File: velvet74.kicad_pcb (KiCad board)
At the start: 4 copper layers, 268 x 133.2 mm, 415 parts, among them J1 Connector, USB-TYPE-C-16P, J2 Connector, USB-TYPE-C-16P, J201 Connector, USB-TYPE-C-16P, J202 Connector, USB-TYPE-C-16P, J203 OLED 128x32, J3 OLED 128x32, SW1 BOOT, SW10 F0, SW11 F1, SW12 F2, SW13 F3, SW14 F4, SW15 F5, SW16 F6 Choc/EC11, SW2 RESET, SW20 N0, SW201 BOOT, SW202 RESET, SW21 N1, SW210 F0, SW211 F1, SW212 F2, SW213 F3, SW214 F4, SW215 F5, SW216 F6 Choc/EC11, SW22 N2, SW220 N0, SW221 N1, SW222 N2, SW223 N3, SW224 N4, SW225 N5, SW23 N3, SW230 T0, SW231 T1, SW232 T2, SW233 T3, SW234 T4, SW235 T5, SW24 N4, SW240 H0, SW241 H1, SW242 H2, SW243 H3, SW244 H4, SW245 H5, SW25 N5, SW250 B0, SW251 B1, SW252 B2, SW253 B3, SW254 B4, SW255 B5, SW260 TH0, SW261 TH1, SW262 TH2, SW263 TH3, SW264 TH4, SW265 TH5 Choc/EC11, SW30 T0, SW31 T1, SW32 T2, SW33 T3, SW34 T4, SW35 T5, SW40 H0, SW41 H1, SW42 H2, SW43 H3, SW44 H4, SW45 H5, SW50 B0, SW51 B1, SW52 B2, SW53 B3, SW54 B4, SW55 B5, SW60 TH0, SW61 TH1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

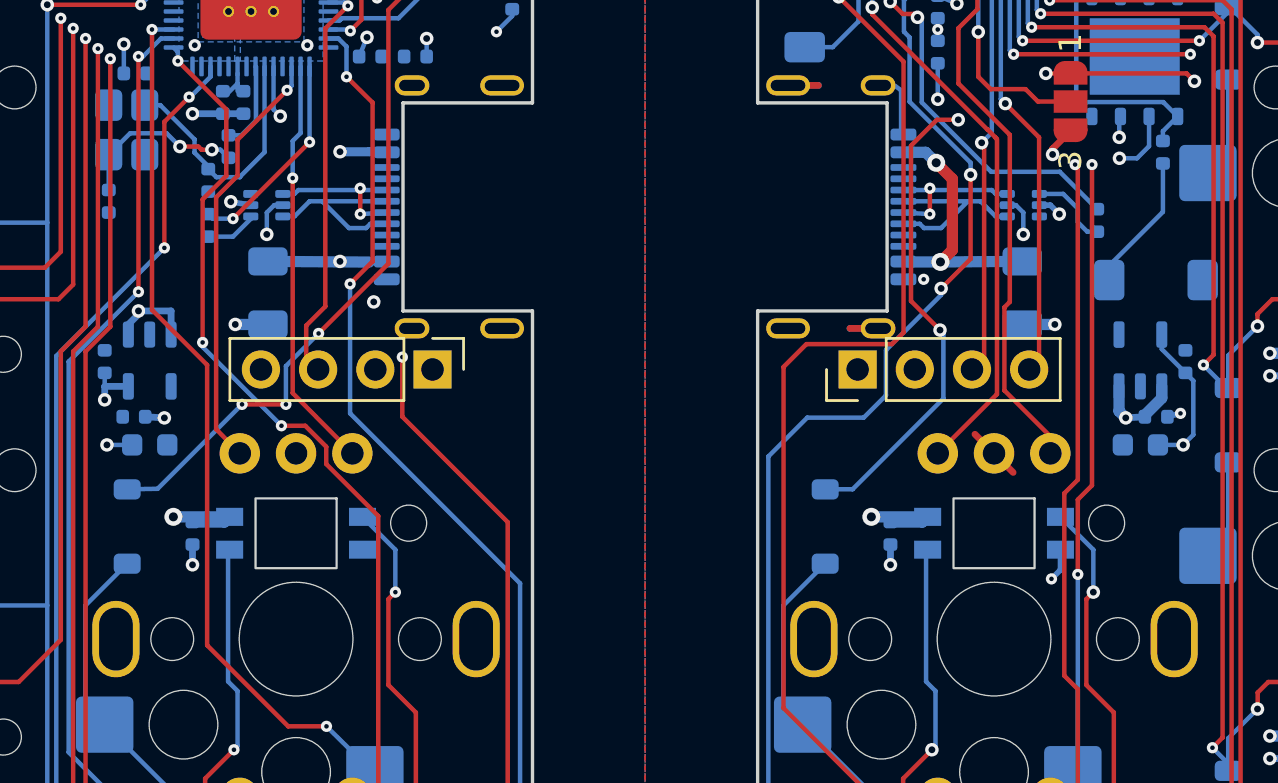
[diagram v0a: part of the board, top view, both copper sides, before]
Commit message: feat(pcb): line the screen up over the encoder column
The OLED now sits over the encoder column on both halves, as on
Keebart's board, so the screen opening and the encoder cutout share a
centre line (107.71 against 108 mm).

- J3 moves one 2.54 mm pin pitch toward the key field: the routing
  lanes between the header pins stay lanes, where the exact 2.25 mm
  would have put every pad on one
- Re-routed J3's GP6/GP7 stubs, GP14/GP18/GP20 at the new pin 4 and
  R4's via off pin 1; both +3.3V In1 island arms reshaped to feed the
  new pin 2
- Plate screen opening, spacer pocket and prototype STLs follow the new
  oled_header point; both fab sets regenerated (only gerbers and drill
  change, J3 is hand-soldered)

DRC with parity: 42 known items, 0 unconnected, 0 parity. ERC 0. No new
via-to-pad gaps, no copper changed outside the two header areas.
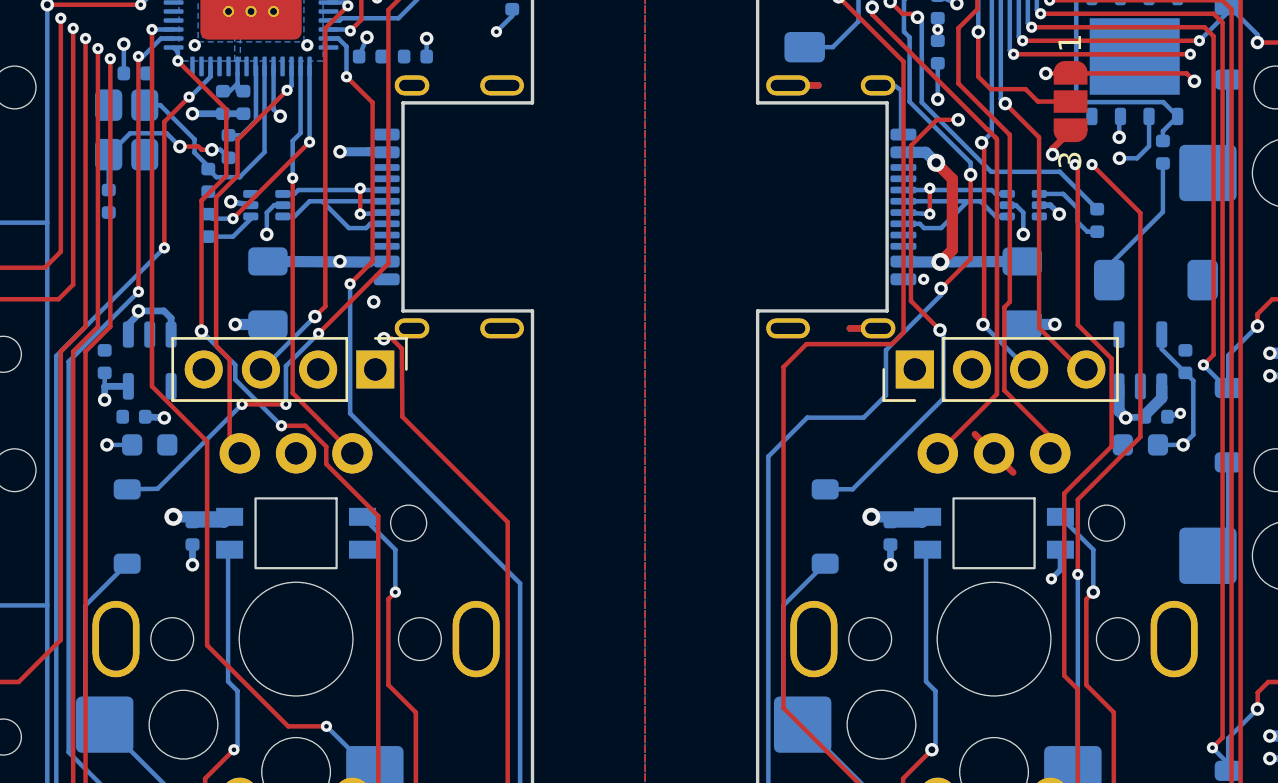
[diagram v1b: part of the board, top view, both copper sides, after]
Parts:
- moved J203 2.54 mm to (195.5, 100.9)
- moved J3 2.54 mm to (171.5, 100.9)
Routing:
- net /Right/GP20: track 49.4 -> 51.2 mm
- net /Right/GP18: track 57.0 -> 58.2 mm
- net /Left/GP6: track 23.2 -> 24.1 mm
- net /Right/GP6: track 18.8 -> 19.7 mm
- net Net-(R4-Pad1): track 100.1 -> 100.8 mm
- net /Right/GP7: track 18.4 -> 19.1 mm, vias 1 -> 2
- net /Left/GP7: track 18.1 -> 18.7 mm, vias 1 -> 2
